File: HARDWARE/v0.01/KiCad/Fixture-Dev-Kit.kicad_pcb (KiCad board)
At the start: 2 copper layers, 379 parts, among them J1 POWER, J10 LED_3, J100 INA_43, J101 INA_43, J102 INA_41, J103 INA_43, J104 INA, J105 INA, J106 LED_6, J107 LED_7, J11 SW_5, J12 LED_4, J13 SW_6, J14 LED_5, J15 SW_7, J16 ADS_48, J17 ADS_48, J18 ADS_4A, J19 ADS_4A, J2 LED_0, J20 ADS_48, J21 ADS_4A, J22 ADS, J23 ADS, J24 ADS_49, J25 ADS_49, J26 ADS_49, J27 ADS_4B, J28 ADS_4B, J29 ADS_4B, J3 SW_0, J30 LOAD_0, J31 LOAD_1, J32 LOAD_2, J33 LOAD_3, J34 Conn_01x20, J35 BAT, J36 CHIP4LH, J38 Conn_01x20, J39 VBUS, J4 SW_1, J40 VBUS, J41 B_D+, J42 D-TP's, J43 B_D-, J44 USB_ID, J45 UPDATE, J46 ANT--SELECT, J47 Conn_01x20, J49 VBUS, J5 LED_1, J50 A_D+, J51 A_D-, J52 CHIP4RH, J53 Conn_01x20, J54 Conn_01x35, J56 Conn_01x35, J57 IOExp_0, J58 IOExp_0, J59 Conn_01x24, J6 SW_2, J60 IOExp_0, J61 IOExp_0, J62 Conn_01x24, J63 FET_0, J64 FET_0, J65 FET_0, J66 FET_0, J67 FET_0, J68 FET_0, J69 FET_0, J7 LED_2, J70 FET_0, J71 NFET_0, J72 NFET_4, J73 NFET_1, J74 NFET_5, J75 NFET_2, J76 NFET_6, J77 NFET_3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

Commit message: pcb roughly 15cm x 15cm
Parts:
- J89: footprint Pin_Headers:Pin_Header_Straight_2x19_Pitch2.54mm -> Pin_Headers:Pin_Header_Straight_2x20_Pitch2.54mm
- moved J53 205.8 mm to (82.8, 145.9), turned to 270 degrees
- moved J47 202.3 mm to (82.8, 143.4), turned to 270 degrees
- moved J52 188.3 mm to (82.8, 133.2), turned to 270 degrees
- moved J35 162.0 mm to (97.0, 143.9), turned to 0 degrees
- moved TP13 159.5 mm to (142.2, 103.2)
- moved TP16 158.0 mm to (141.7, 113.4)
- moved TP17 157.9 mm to (141.7, 115.9)
- moved TP19 152.9 mm to (141.7, 123.6)
- moved TP15 152.4 mm to (142.2, 108.3)
- moved Q1 152.3 mm to (136.7, 105.8), turned to 180 degrees
- moved TP18 149.7 mm to (141.7, 118.5)
- moved TP14 149.3 mm to (142.2, 105.8)
- moved TP24 147.0 mm to (141.7, 139.3)
- moved TP22 146.3 mm to (141.7, 134.2)
- moved J36 143.0 mm to (82.8, 100.2), turned to 270 degrees
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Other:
- board outline added: 151.4 x 138.2 mm
- board text added: "BUTTONS"
- board text added: "LED's"

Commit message: more PCB layout
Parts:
- added J37: USB_OTG, Connectors_USB:USB_Micro-B_Molex_47346-0001, F.Cu at (106.7, 163.1)
- moved R73 320.6 mm to (105.5, 49.4), turned to 90 degrees
- moved R71 318.0 mm to (105.6, 35.0), turned to 90 degrees
- moved R74 317.3 mm to (105.5, 44.6), turned to 90 degrees
- moved R75 315.7 mm to (105.5, 54.1), turned to 90 degrees
- moved R69 314.1 mm to (105.6, 30.3), turned to 90 degrees
- moved R72 313.3 mm to (105.5, 39.8), turned to 90 degrees
- moved R80 313.3 mm to (105.5, 77.9), turned to 90 degrees
- moved R78 309.4 mm to (105.5, 63.6), turned to 90 degrees
- moved R82 305.8 mm to (105.5, 82.7), turned to 90 degrees
- moved Q14 304.2 mm to (108.3, 32.3), turned to 180 degrees
- moved R77 302.1 mm to (105.5, 73.2), turned to 90 degrees
- moved R83 301.2 mm to (105.5, 92.2), turned to 90 degrees
- moved Q17 299.2 mm to (108.1, 61.2), turned to 180 degrees
- moved R76 298.3 mm to (105.5, 58.9), turned to 90 degrees
- moved R79 296.4 mm to (105.5, 68.4), turned to 90 degrees
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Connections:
- J16 pad 1: /Fixture Dev Kit - ADS/I2C-SCK -> /Fixture Dev Kit - ADS/C4-VCC-3V3
- J16 pad 2: /Fixture Dev Kit - ADS/I2C-SDA -> GND
- J16 pad 3: GND -> /Fixture Dev Kit - ADS/I2C-SDA
- J16 pad 4: /Fixture Dev Kit - ADS/C4-VCC-3V3 -> /Fixture Dev Kit - ADS/I2C-SCK
- J17 pad 1: /Fixture Dev Kit - ADS/I2C-SCK -> /Fixture Dev Kit - ADS/C4-VCC-3V3
- J17 pad 2: /Fixture Dev Kit - ADS/I2C-SDA -> GND
- J17 pad 3: GND -> /Fixture Dev Kit - ADS/I2C-SDA
- J17 pad 4: /Fixture Dev Kit - ADS/C4-VCC-3V3 -> /Fixture Dev Kit - ADS/I2C-SCK
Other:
- board text added: "1"
- board text added: "2"
- board text added: "3"
- board text added: "4"
- board text removed: "ADS CIRCUITS"
- board text removed: "INA CIRCUITS"

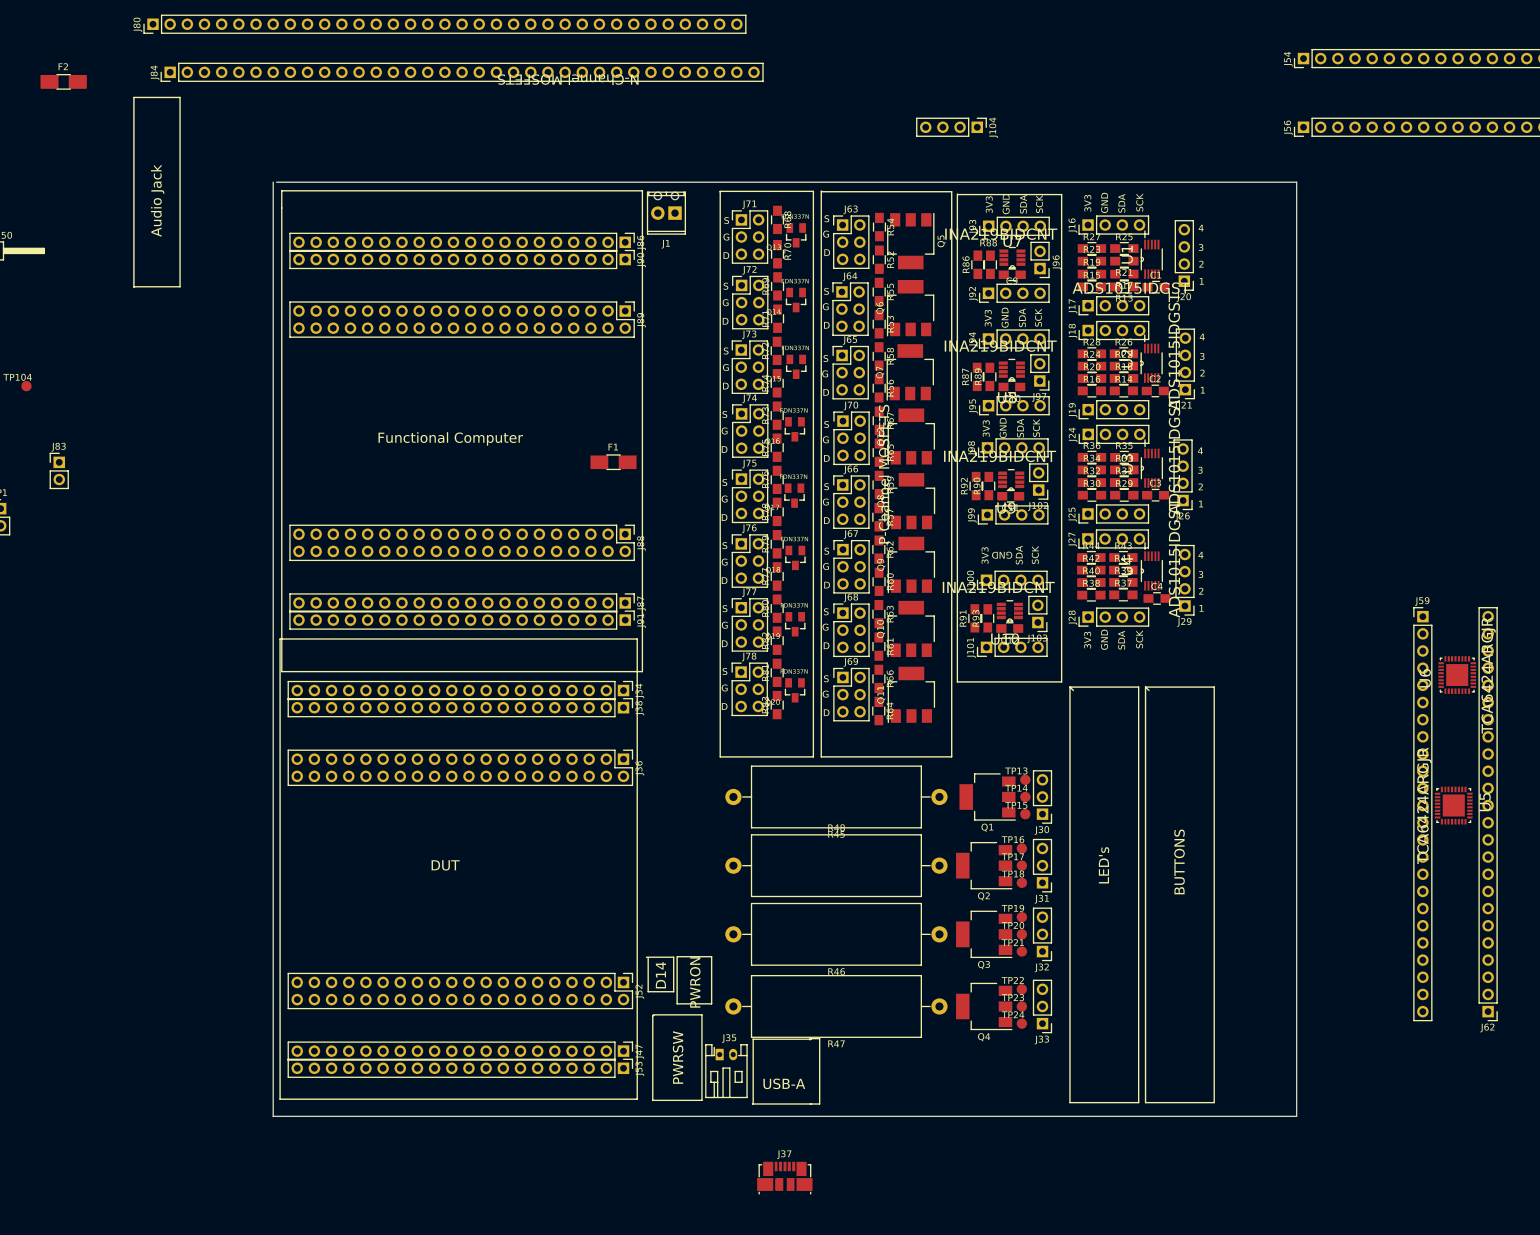
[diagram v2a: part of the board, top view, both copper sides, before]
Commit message: adding datasheets and laying out PCB
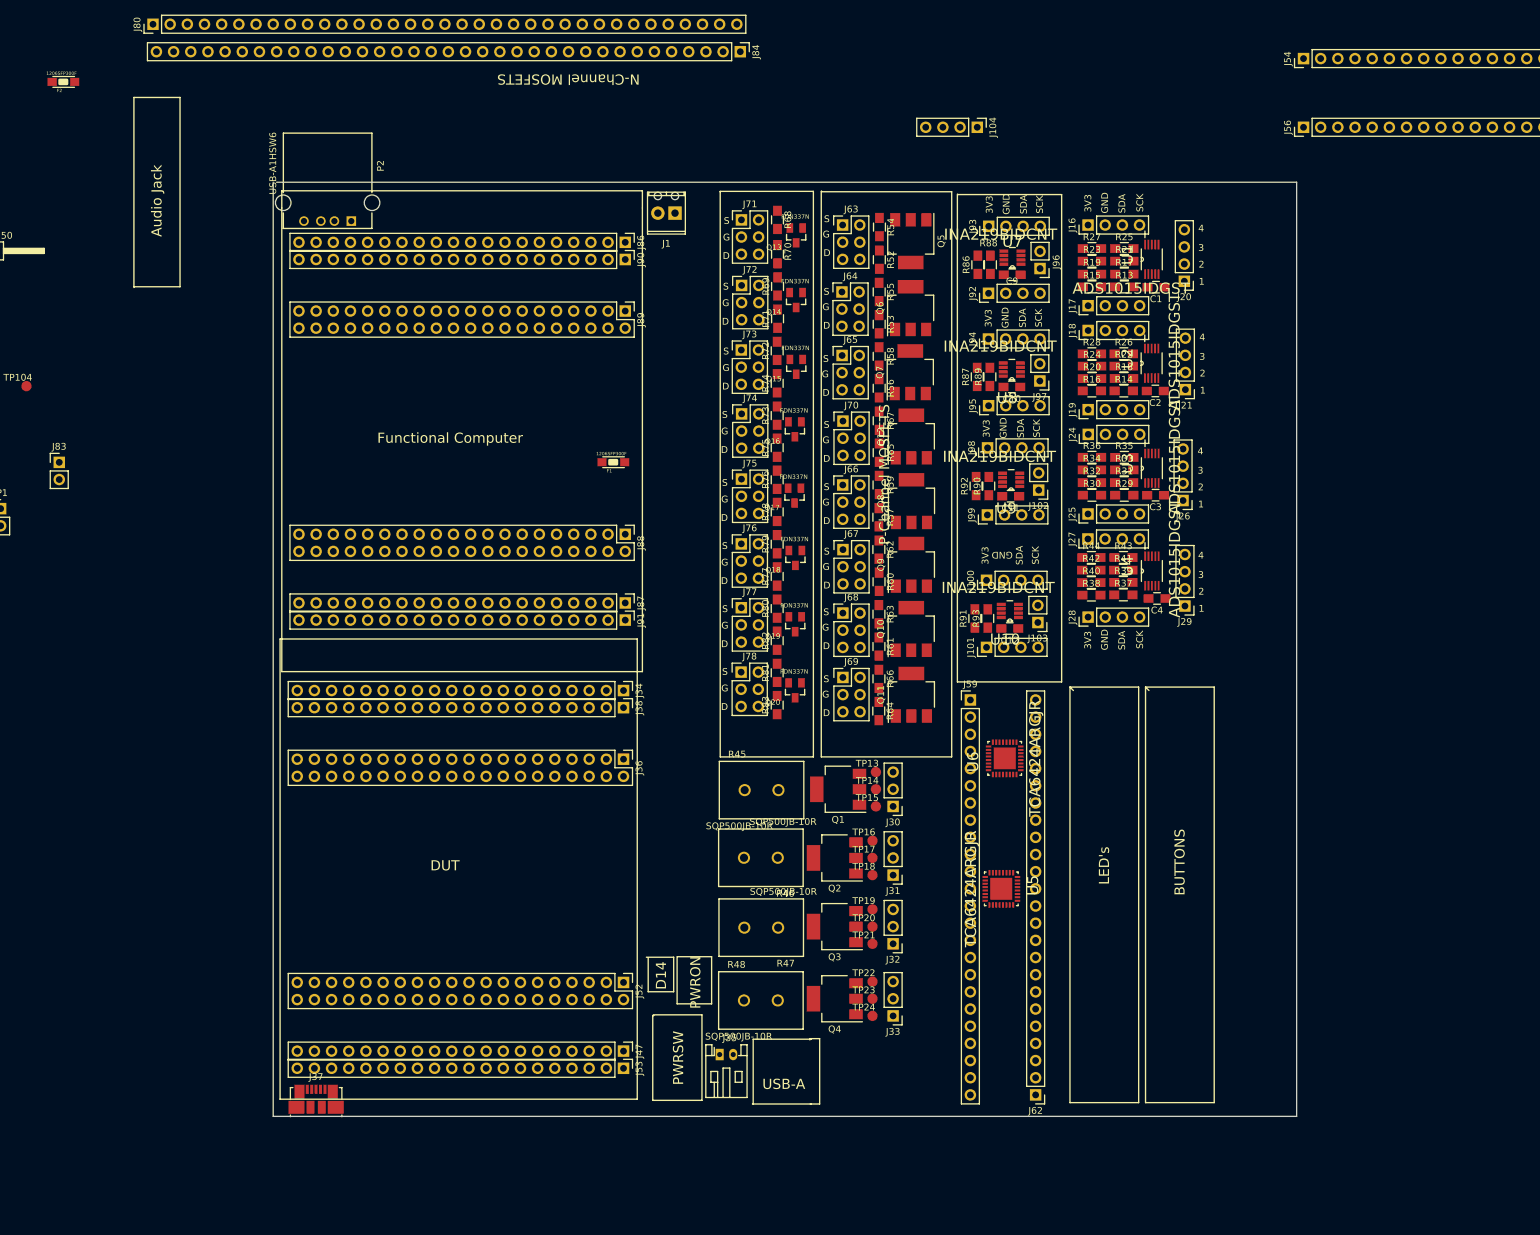
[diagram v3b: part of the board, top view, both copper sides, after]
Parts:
- added P2: USB-A1HSW6, USB-A1HSW6:OST_USB-A1HSW6, F.Cu at (39.0, 14.1)
- F1, F2: footprint Fuse_Holders_and_Fuses:Fuse_SMD1206_HandSoldering -> 1206:1206
- R45, R46, R47, R48: value 10R, 5W -> SQP500JB-10R; footprint Resistors_THT:R_Axial_Power_L25.0mm_W9.0mm_P30.48mm -> RES_TWM3J560E:RES_TWM3J560E
- moved J84 84.4 mm to (100.1, -4.46), turned to 270 degrees
- moved J37 70.3 mm to (37.3, 151.7)
- moved J59 68.1 mm to (134.1, 91.4)
- moved J62 68.1 mm to (143.8, 149.8)
- moved U5 68.1 mm to (138.7, 119.4)
- moved U6 68.1 mm to (139.2, 100.1)
- moved R47 28.8 mm to (103.2, 125.1)
- moved R46 28.7 mm to (103.1, 114.8)
- moved R45 26.3 mm to (103.2, 104.8), turned to 0 degrees
- moved J30 22.1 mm to (122.7, 107.2)
- moved J31 22.1 mm to (122.7, 117.3)
- moved J32 22.1 mm to (122.7, 127.5)
- moved J33 22.1 mm to (122.7, 138.2)
- moved TP16 22.1 mm to (119.6, 112.2)
- moved TP17 22.1 mm to (119.6, 114.8)
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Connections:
- J63 pad 5: Net-(J63-Pad5) -> /Fixture Dev Kit - PMosfets/Drain0
- J64 pad 5: Net-(J64-Pad5) -> /Fixture Dev Kit - PMosfets/Drain4
- J65 pad 5: Net-(J65-Pad5) -> /Fixture Dev Kit - PMosfets/Drain1
- J66 pad 5: Net-(J66-Pad5) -> /Fixture Dev Kit - PMosfets/Drain5
- J67 pad 5: Net-(J67-Pad5) -> /Fixture Dev Kit - PMosfets/Drain2
- J68 pad 5: Net-(J68-Pad5) -> /Fixture Dev Kit - PMosfets/Drain6
- J69 pad 5: Net-(J69-Pad5) -> /Fixture Dev Kit - PMosfets/Drain3
- J70 pad 5: Net-(J70-Pad5) -> /Fixture Dev Kit - PMosfets/Drain7
